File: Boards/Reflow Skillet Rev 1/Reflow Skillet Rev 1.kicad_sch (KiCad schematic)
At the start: 2 parts

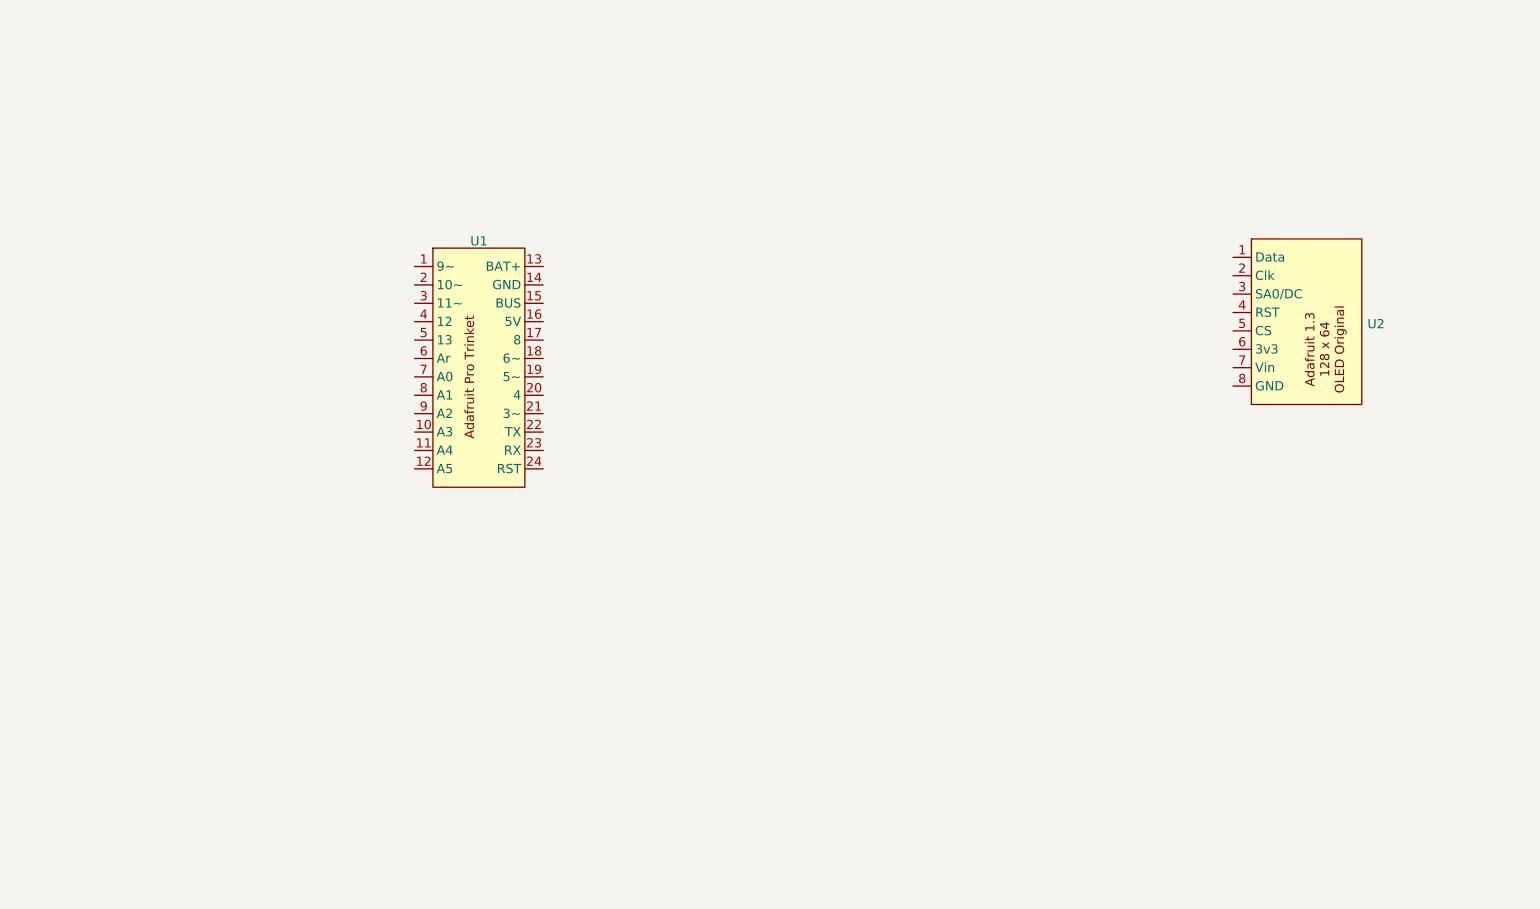
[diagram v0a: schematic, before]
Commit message: Board before routing
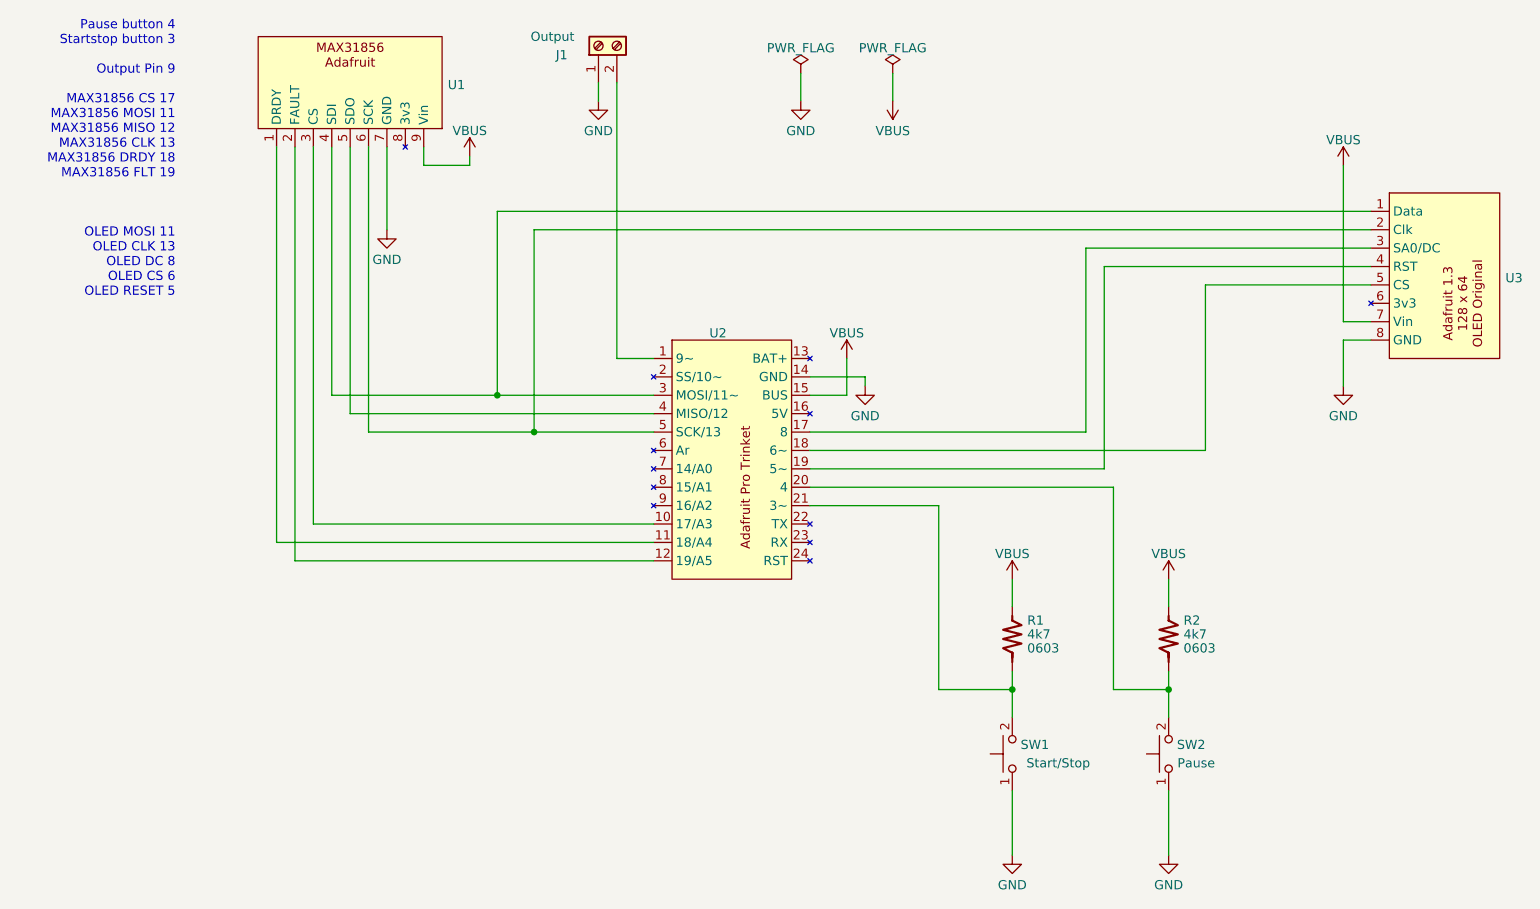
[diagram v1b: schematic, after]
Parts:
- added J1: Output, TerminalBlock_TE-Connectivity:TerminalBlock_TE_282834-2_1x02_P2.54mm_Horizontal, symbol MyConnectors:Screw_Terminal_01x02 TE 282834-2
- added R1, R2: 4k7, Resistor_SMD:R_0603_1608Metric_Pad0.98x0.95mm_HandSolder, symbol MyResistors:R_vert
- added SW1: Start/Stop, Button_Switch_THT:SW_TH_Tactile_Omron_B3F-10xx, symbol Switch:SW_Push
- added SW2: Pause, Button_Switch_THT:SW_TH_Tactile_Omron_B3F-10xx, symbol Switch:SW_Push
- added U1: ~, MyBoards:Adafruit MAX31856, symbol MyBoards:Adafruit_MAX31856
- U2: renamed from U1; footprint (none) -> MyBoards:Adafruit Pro Trinket
- U3: renamed from U2; footprint (none) -> MyBoards:Adafruit 1.3 128 x 64 OLED Original
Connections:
- net at U2.1 (9~): now also J1.2 (Pin_2)
- net at U2.10 (17/A3): now also U1.3 (CS)
- net at U2.11 (18/A4): now also U1.1 (DRDY)
- net at U2.12 (19/A5): now also U1.2 (FAULT)
- net GND: now reaches U2.14 (GND)
- net GND: now also U3.8 (GND), J1.1 (Pin_1), SW1.1, SW2.1, U1.7 (GND)
- net VBUS: now reaches U2.15 (BUS)
- net VBUS: now also U3.7 (Vin), R1.1, R2.1, U1.9 (Vin)
- net at U2.17 (8): now also U3.3 (SA0/DC)
- net at U2.18 (6~): now also U3.5 (CS)
- net at U2.19 (5~): now also U3.4 (RST)
- net at U2.20 (4): now also R2.2, SW2.2
- net at U2.21 (3~): now also R1.2, SW1.2
- net at U2.3 (MOSI/11~): now also U3.1 (Data), U1.4 (SDI)
- net at U2.4 (MISO/12): now also U1.5 (SDO)
- net at U2.5 (SCK/13): now also U3.2 (Clk), U1.6 (SCK)
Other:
- note added: "Pause button 4 Startstop button 3 Output Pin 9 MAX31856 CS 17 MAX31856 MOSI 11 MAX31856 MISO 12 MAX31856 CLK 13 MAX31856 DRDY 18 MAX31856 FLT 19 OLED MOSI 11 OLED CLK 13 OLED DC 8 OLED CS 6 OLED RESET 5"
